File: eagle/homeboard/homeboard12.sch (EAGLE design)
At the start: 115 parts, among them IC1 XCF02S, IC2 25LC080SN, IC3 ATMEGA32U2-TQFP, Q5 BC848SMD, Q6 BC848SMD, Q7 BC848SMD, Q8 BC848SMD, T1 BSS138, T2 BC848, T3 BSS138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

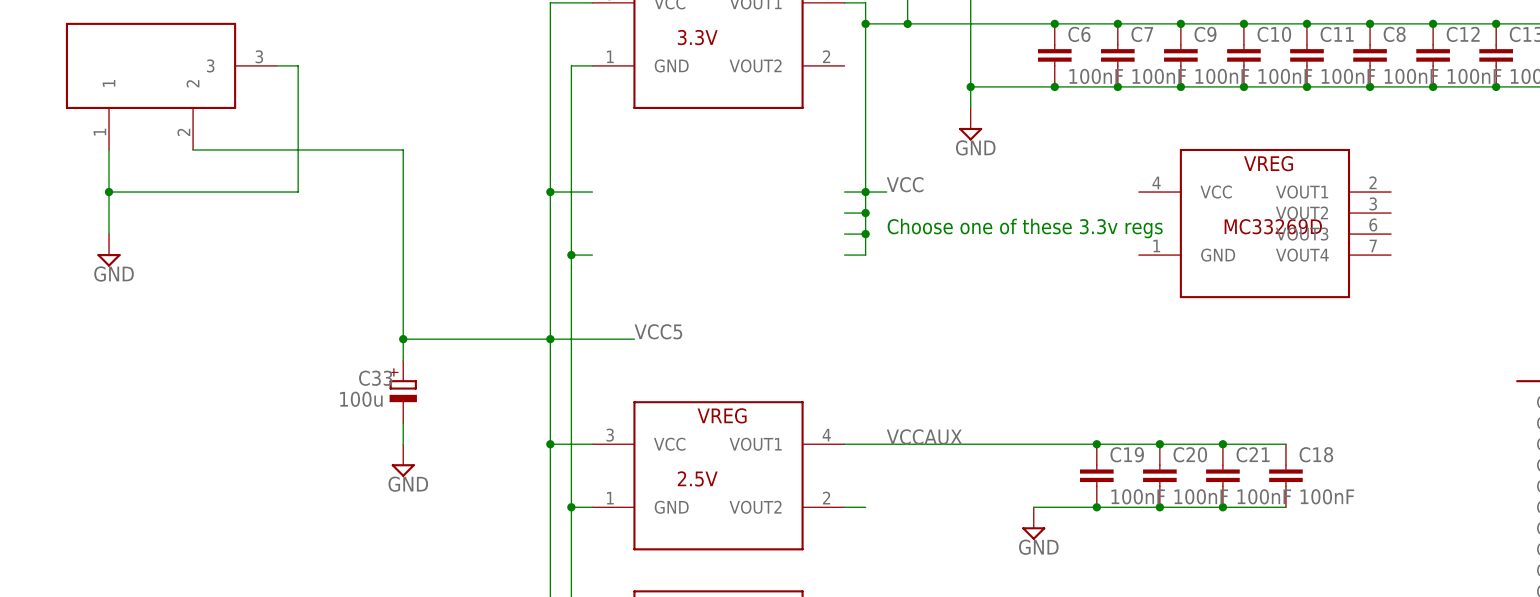
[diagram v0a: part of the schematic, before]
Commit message: re-added mc33269
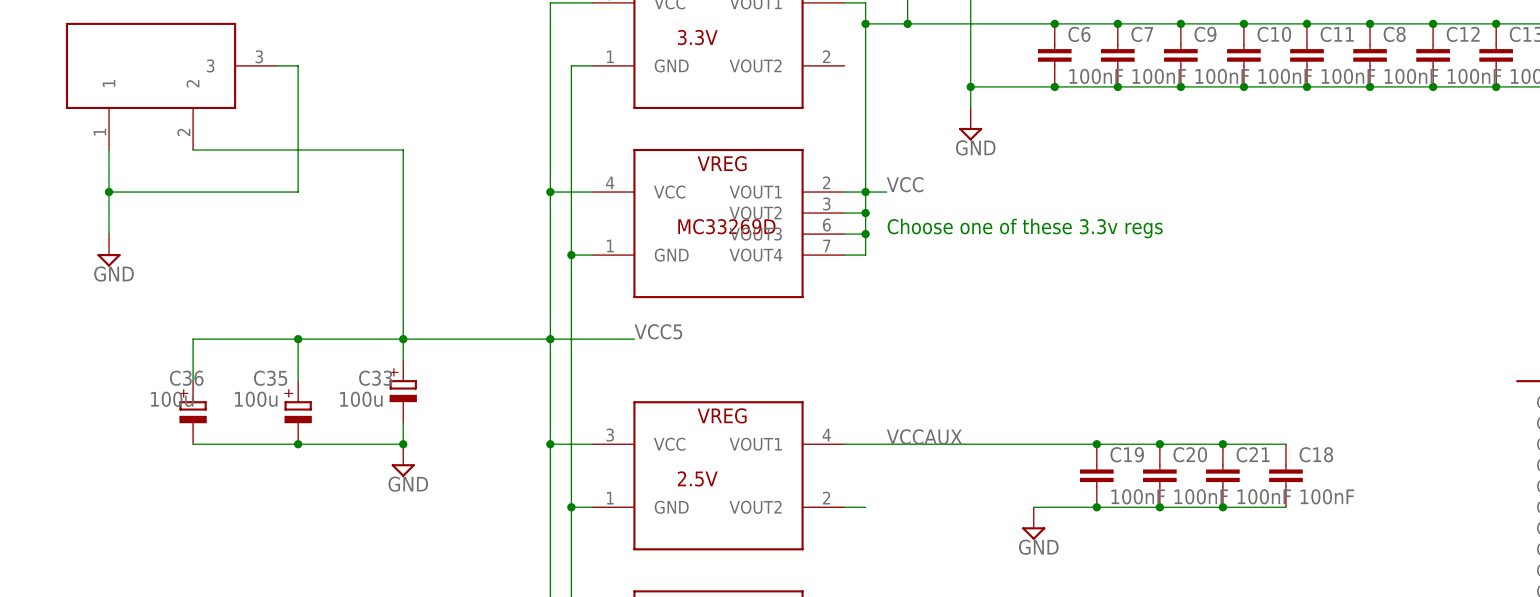
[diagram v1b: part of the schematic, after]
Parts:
- added C35, C36: 100u, rcl:CPOL-EUD
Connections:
- net GND: now also C35.-, C36.-, U$5.GND
- net VCC: now also U$5.VOUT1, U$5.VOUT2, U$5.VOUT3, U$5.VOUT4
- net VCC5: now also C35.+, C36.+, U$5.VCC
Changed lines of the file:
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@@
 <part name="U$6" library="cpcfpga" deviceset="AS6C4008" device=""/>
 <part name="C34" library="rcl" deviceset="C-EU" device="C0603" value="100nF"/>
+<part name="C35" library="rcl" deviceset="CPOL-EU" device="D" value="100u"/>
+<part name="C36" library="rcl" deviceset="CPOL-EU" device="D" value="100u"/>
 </parts>
 <sheets>
@@
 </instance>
 <instance part="SUPPLY14" gate="GND" x="-226.06" y="58.42"/>
-<instance part="U$5" gate="G$1" x="-121.92" y="86.36"/>
+<instance part="U$5" gate="G$1" x="-187.96" y="86.36"/>
 <instance part="SUPPLY15" gate="GND" x="48.26" y="-43.18"/>
 <instance part="U$6" gate="G$1" x="45.72" y="20.32" rot="MR270"/>
 <instance part="C34" gate="G$1" x="-93.98" y="127"/>
+<instance part="C35" gate="G$1" x="-238.76" y="66.04" smashed="yes">
+<attribute name="NAME" x="-244.221" y="68.0466" size="1.778" layer="95"/>
+<attribute name="VALUE" x="-246.634" y="65.5066" size="1.778" layer="96"/>
+</instance>
+<instance part="C36" gate="G$1" x="-251.46" y="66.04" smashed="yes">
+<attribute name="NAME" x="-254.381" y="68.0466" size="1.778" layer="95"/>
+<attribute name="VALUE" x="-256.794" y="65.5066" size="1.778" layer="96"/>
+</instance>
 </instances>
 <busses>
@@
 <wire x1="-205.74" y1="106.68" x2="-205.74" y2="83.82" width="0.1524" layer="91"/>
 <junction x="-205.74" y="83.82"/>
+<pinref part="U$5" gate="G$1" pin="GND"/>
 </segment>
 <segment>
@@
 <pinref part="C33" gate="G$1" pin="-"/>
 <wire x1="-226.06" y1="60.96" x2="-226.06" y2="63.5" width="0.1524" layer="91"/>
+<pinref part="C36" gate="G$1" pin="-"/>
+<pinref part="C35" gate="G$1" pin="-"/>
+<wire x1="-251.46" y1="60.96" x2="-238.76" y2="60.96" width="0.1524" layer="91"/>
+<wire x1="-238.76" y1="60.96" x2="-226.06" y2="60.96" width="0.1524" layer="91"/>
+<junction x="-238.76" y="60.96"/>
+<junction x="-226.06" y="60.96"/>
 </segment>
 <segment>
@@
 <wire x1="-93.98" y1="129.54" x2="-101.6" y2="129.54" width="0.1524" layer="91"/>
 <junction x="-101.6" y="129.54"/>
+<pinref part="U$5" gate="G$1" pin="VOUT1"/>
+<pinref part="U$5" gate="G$1" pin="VOUT4"/>
+<pinref part="U$5" gate="G$1" pin="VOUT2"/>
+<pinref part="U$5" gate="G$1" pin="VOUT3"/>
 </segment>
 <segment>
@@
 <wire x1="-226.06" y1="71.12" x2="-226.06" y2="73.66" width="0.1524" layer="91"/>
 <junction x="-226.06" y="73.66"/>
-</segment>
-</net>
+<pinref part="U$5" gate="G$1" pin="VCC"/>
+<pinref part="C35" gate="G$1" pin="+"/>
+<wire x1="-226.06" y1="73.66" x2="-238.76" y2="73.66" width="0.1524" layer="91"/>
+<wire x1="-238.76" y1="73.66" x2="-238.76" y2="68.58" width="0.1524" layer="91"/>
+<pinref part="C36" gate="G$1" pin="+"/>
+<wire x1="-238.76" y1="73.66" x2="-251.46" y2="73.66" width="0.1524" layer="91"/>
+<wire x1="-251.46" y1="73.66" x2="-251.46" y2="68.58" width="0.1524" layer="91"/>
+<junction x="-238.76" y="73.66"/>
+</segment>
+</net>
